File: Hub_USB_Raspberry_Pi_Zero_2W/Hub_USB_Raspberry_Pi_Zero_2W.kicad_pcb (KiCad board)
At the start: 4 copper layers, 65 x 30 mm, 51 parts, among them J1 USB_C_Receptacle_USB2.0_16P, J2 USB_C_Receptacle_USB2.0_16P, J3 USB_C_Receptacle_USB2.0_16P, J4 USB_C_Receptacle_USB2.0_16P, U1 USBLC6-2SC6, U2 USBLC6-2SC6, U3 USBLC6-2SC6, U4 USBLC6-2SC6, U5 24C02Cx-x-SN, U6 CH334F, Y1 12 MHZ

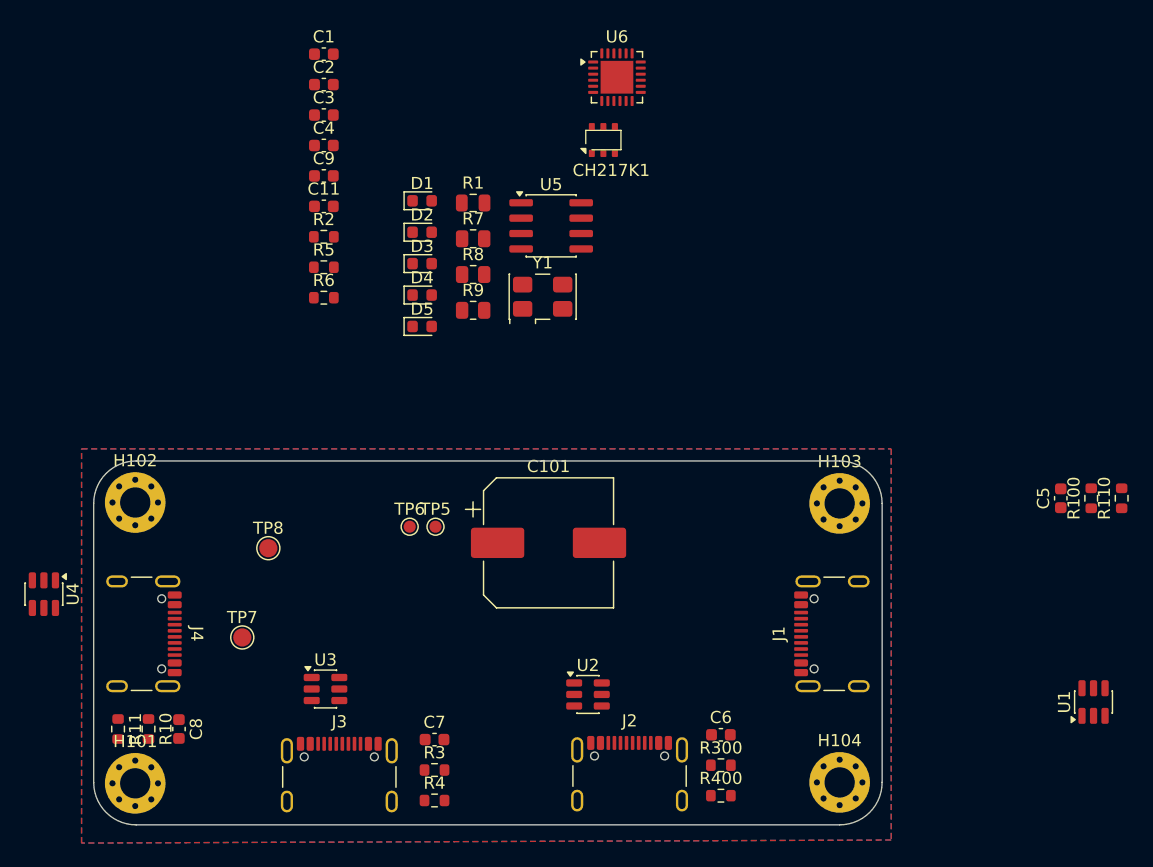
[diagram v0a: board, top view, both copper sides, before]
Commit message: Finalisation Routage PCB HUB
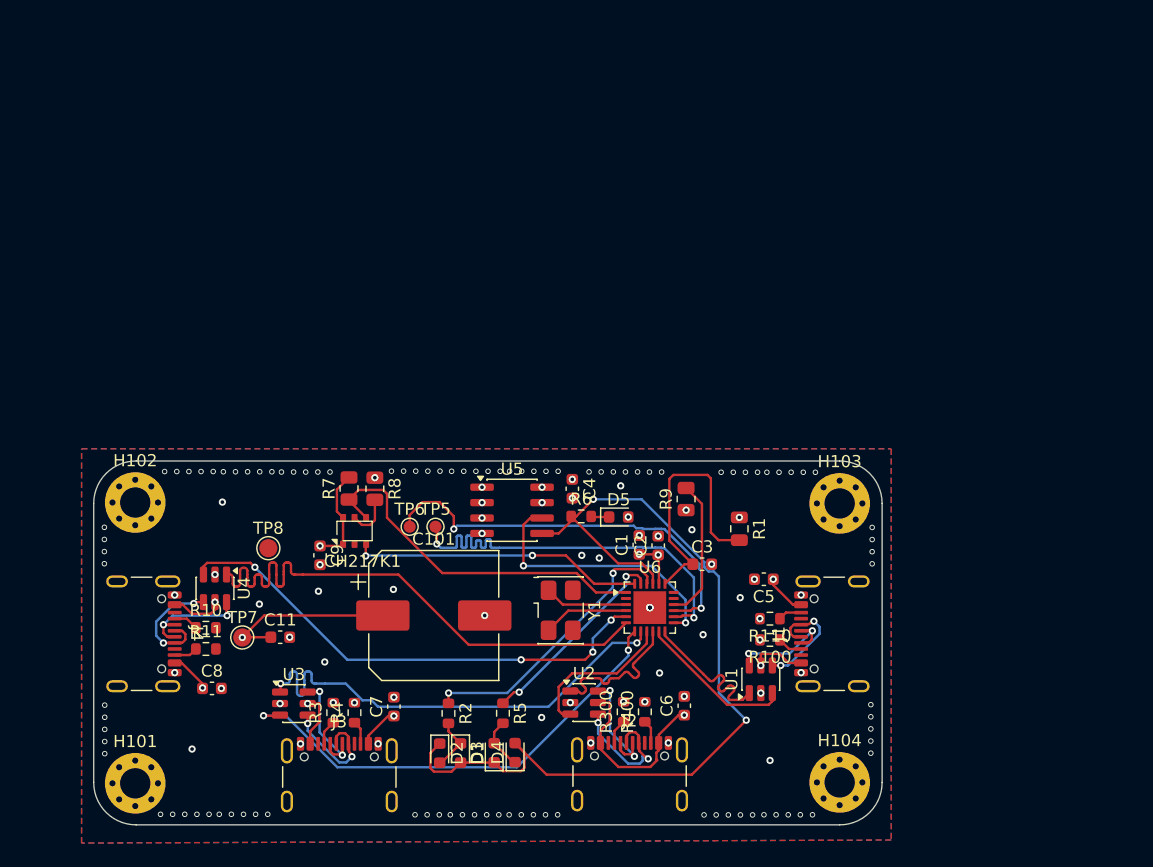
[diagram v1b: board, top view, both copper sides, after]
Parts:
- moved C3 48.4 mm to (83.9, 27.0)
- moved C1 48.1 mm to (78.7, 25.4), turned to 90 degrees
- moved C2 46.9 mm to (80.3, 25.5), turned to 90 degrees
- moved D1 45.6 mm to (64.0, 42.6), turned to -90 degrees
- moved U6 43.8 mm to (79.6, 30.6)
- moved D2 43.0 mm to (62.3, 42.6), turned to -90 degrees
- moved D3 40.8 mm to (66.8, 42.6), turned to 90 degrees
- moved R2 40.6 mm to (63.0, 39.3), turned to -90 degrees
- moved R5 39.6 mm to (67.5, 39.3), turned to -90 degrees
- moved D4 38.5 mm to (68.5, 42.5), turned to 90 degrees
- moved CH217K1 38.2 mm to (53.8, 23.5)
- moved C11 35.7 mm to (49.1, 33.0)
- moved C4 34.9 mm to (73.2, 20.8), turned to -90 degrees
- moved R1 34.7 mm to (87.0, 24.1), turned to -90 degrees
- moved C9 31.3 mm to (52.4, 26.3), turned to -90 degrees
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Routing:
- net /USB HUB controller/LED4/SDA: track 0.00 -> 77.2 mm, vias 0 -> 2
- net +5V: track 0.00 -> 62.2 mm, vias 0 -> 11
- net /USB HUB controller/DP4+: track 0.00 -> 47.2 mm
- net /USB HUB controller/DM4-: track 0.00 -> 41.1 mm, vias 0 -> 4
- net /USB HUB controller/DM3-: track 0.00 -> 39.3 mm, vias 0 -> 2
- net /USB HUB controller/DP3+: track 0.00 -> 39.2 mm, vias 0 -> 2
- net Net-(U6-DMU-): track 0.00 -> 34.8 mm, vias 0 -> 2
- net Net-(U6-DPU+): track 0.00 -> 34.3 mm, vias 0 -> 2
- net /USB HUB controller/OVCUR#: track 0.00 -> 29.9 mm
- net /USB HUB controller/~{PWREN}: track 0.00 -> 24.1 mm, vias 0 -> 2
- net /USB HUB controller/LED1: track 0.00 -> 23.1 mm, vias 0 -> 2
- net /USB HUB controller/LED3/SCL: track 0.00 -> 22.6 mm, vias 0 -> 2
- net Net-(U6-V5): track 0.00 -> 21.5 mm
- net /USB HUB controller/LED2: track 0.00 -> 16.7 mm, vias 0 -> 2
- net /USB HUB controller/DM1-: track 0.00 -> 12.9 mm
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- added copper zone on In1.Cu, net +3V3
- added copper zone on In1.Cu, net +5V
- added copper zone on In2.Cu, net GND
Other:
- board text added: "PCB Edge"
